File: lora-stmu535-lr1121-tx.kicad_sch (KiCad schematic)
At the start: 0 parts

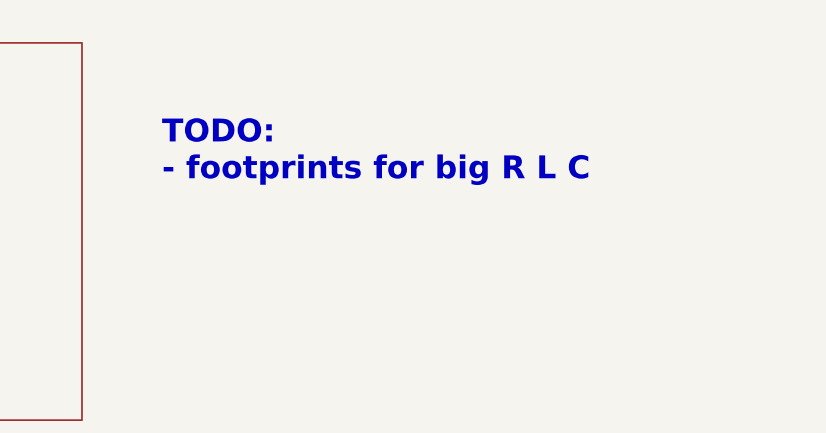
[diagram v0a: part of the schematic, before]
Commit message: labeling and via placing
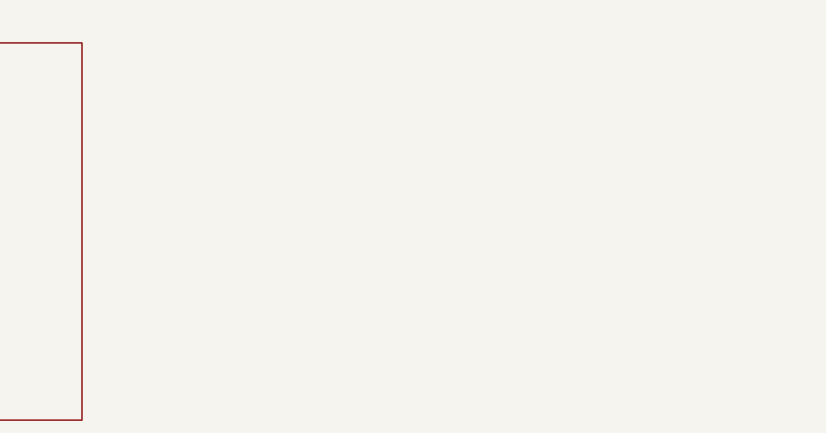
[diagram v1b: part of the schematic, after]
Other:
- note removed: "TODO: - footprints for big R L C"
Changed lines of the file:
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@@
-		)
-	)
-	(text "TODO:\n- footprints for big R L C"
-		(exclude_from_sim no)
-		(at 125.73 51.435 0)
-		(effects
-			(font
-				(size 2.54 2.54)
-				(thickness 0.254)
-				(bold yes)
-			)
-			(justify left)
 		)
 	)
